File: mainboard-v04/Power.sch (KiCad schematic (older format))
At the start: 53 parts, among them Q1 IRLML2803, U17 BQ25883RGER, U4 ADM1176-1ARMZ-R7, U5 TPS54226PWPRPWP14_2P31X2P46-L, U6 LTC4121, U7 NDS8434

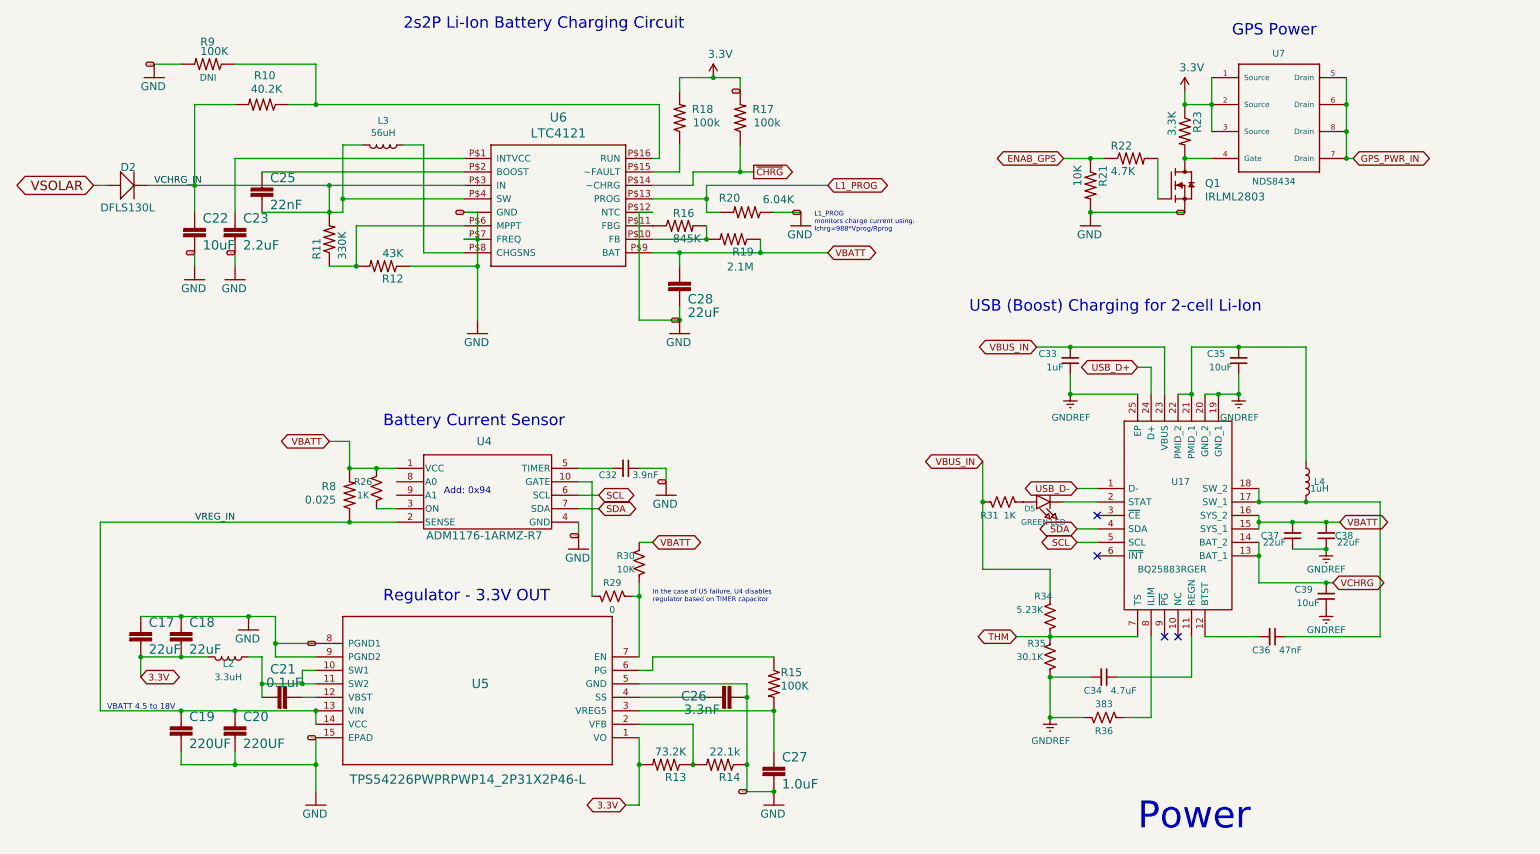
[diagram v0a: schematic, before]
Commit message: adding mainbaordv04 layout and BOM
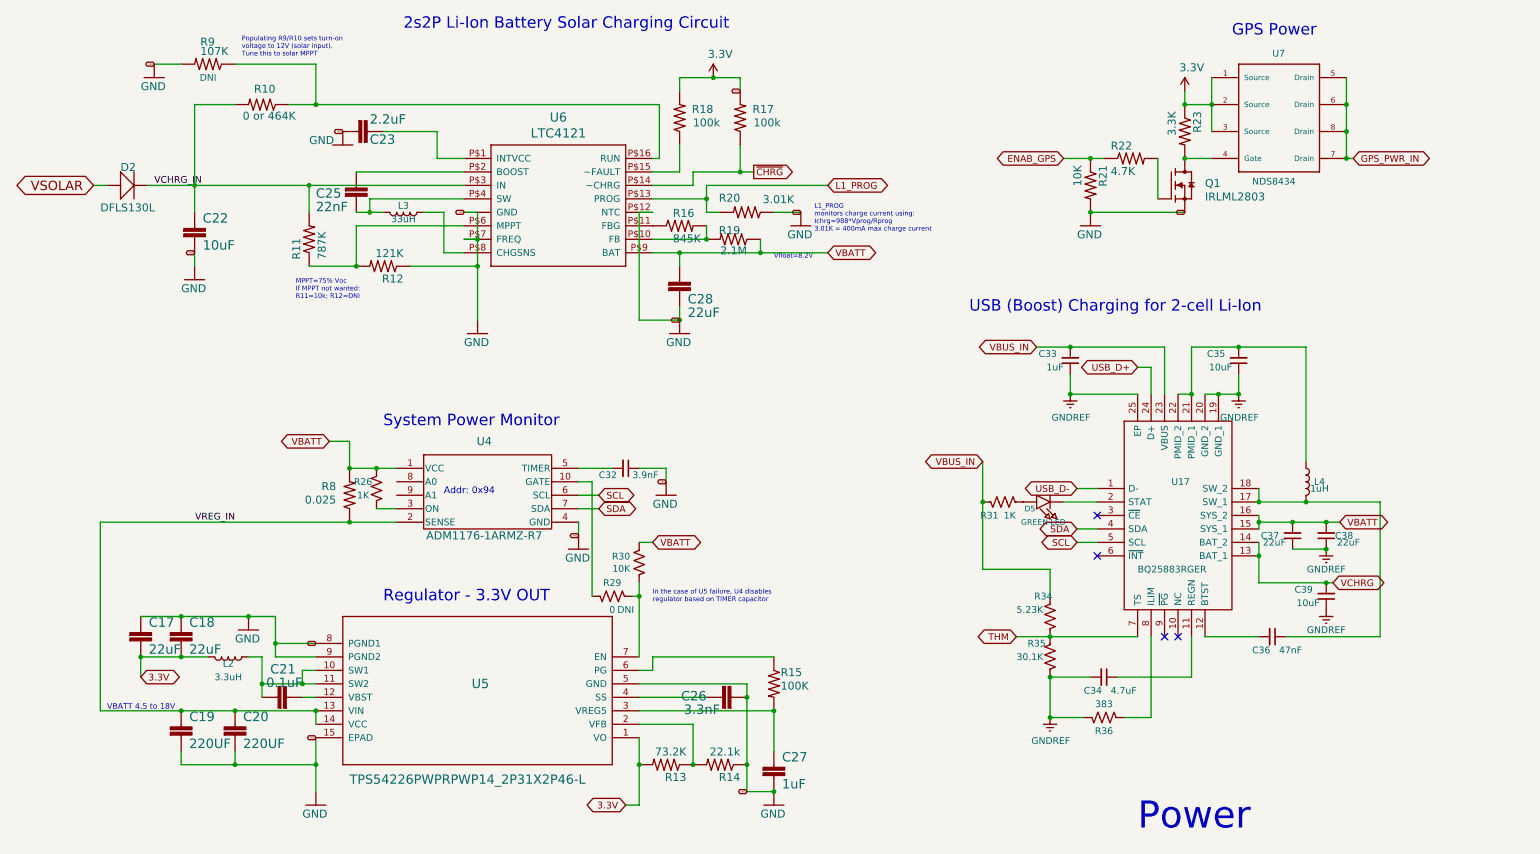
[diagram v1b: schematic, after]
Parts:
- C27: value 1.0uF -> 1uF
- D2: Flight (none) -> DFLS130L; Proto (none) -> DFLS130L
- L2: footprint Inductor_SMD:L_1812_4532Metric -> custom-footprints:L_2141
- L3: value 56uH -> 33uH
- Q1: Flight (none) -> IRLML2803; Proto (none) -> 2302
- R10: value 40.2K -> 0 or 464K
- R11: value 330K -> 787K
- R12: value 43K -> 121K
- R20: value 6.04K -> 3.01K
- R29: DNI (none) -> DNI
- R9: value 100K -> 107K
- U17: Flight (none) -> BQ25883RGER; Height 1 -> (none); Manufacturer_Name Texas Instruments -> (none); Manufacturer_Part_Number BQ25883RGER -> (none); Mouser Part Number 595-BQ25883RGER -> (none); Mouser Price/Stock https://www.mouser.com/Search/Refine.aspx?Keyword=595-BQ258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 -> (none); Proto (none) -> BQ25883RGER
- U4: Flight (none) -> ADM1176-1ARMZ-R7; Proto (none) -> ADM1176-1ARMZ-R7
- U5: Flight (none) -> TPS54226PWPRPWP14_2P31X2P46-L; Proto (none) -> TPS54226PWPRPWP14_2P31X2P46-L
- U6: Flight (none) -> LTC4121EUD; Proto (none) -> LTC4121EUD
- U7: Field4 ON Semiconductor -> (none); Field5 Unavailable -> (none); Field6 None -> (none); Field7 NDS8434 -> (none); Field8 SO-8 ON Semiconductor -> (none); Flight (none) -> NDS8434; Proto (none) -> DMP2022LSS-13
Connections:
- net VCHRG_IN: no longer C25.2, L3.2, U6.P$4 (SW)
- new net: C25.2, L3.2, U6.P$4 (SW)
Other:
- note added: "2s2P Li-Ion Battery Solar Charging Circuit"
- note added: "Addr: 0x94"
- note added: "L1_PROG\nmonitors charge current using:\nIchrg=988*Vprog/Rprog\n3.01K = 400mA max charge current\n"
- note added: "MPPT=75% Voc\nIf MPPT not wanted:\nR11=10k; R12=DNI"
- note added: "Populating R9/R10 sets turn-on\nvoltage to 12V (solar input). \nTune this to solar MPPT"
- note added: "System Power Monitor"
- note added: "Vfloat=8.2V"
- note removed: "2s2P Li-Ion Battery Charging Circuit"
- note removed: "Add: 0x94"
- note removed: "Battery Current Sensor"
- note removed: "L1_PROG\nmonitors charge current using:\nIchrg=988*Vprog/Rprog\n"
- moved on the sheet: C23, C25, L3, R11

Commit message: cleaned up v04
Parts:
- added J14: USB Jumpers, Connector_PinHeader_2.54mm:PinHeader_1x04_P2.54mm_Vertical, symbol Connector_Generic:Conn_01x04
- added R46: 10K, Resistor_SMD:R_0603_1608Metric, symbol Device:R_US
- C19, C20: value 220UF -> 100uF
- L2: Flight (none) -> SPM5030T-3R3M-HZ; Proto (none) -> HPC5040NF-3R3MTH
- L3: Flight (none) -> SLF6028T-330MR69-PF; Proto (none) -> SNR5040K-330M
- L4: footprint custom-footprints:XFL4030472MEB -> custom-footprints:L_4141; Flight (none) -> XFL4020-222ME; PN XFL4020-222ME -> (none); Proto (none) -> XFL4020-222ME
- R10: value 0 or 464K -> 0
- R11: value 787K -> 10K
- R12: DNI (none) -> DNI
- R8: value 0.025 -> 1.0
- U17: footprint QFN50P400X400X100-25N-D -> custom-footprints:QFN50P400X400X100-25N-D
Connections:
- net GNDREF: now also R46.1
- net THM: now also R46.2
- net VBATT: now also J14.2 (Pin_2); no longer C37.2, C38.2, U17.15 (SYS_1), U17.16 (SYS_2)
- net VCHRG: now also J14.4 (Pin_4); no longer C39.2, U17.13 (BAT_1), U17.14 (BAT_2)
- new net: C37.2, C38.2, J14.1 (Pin_1), U17.15 (SYS_1), U17.16 (SYS_2)
- new net: C39.2, J14.3 (Pin_3), U17.13 (BAT_1), U17.14 (BAT_2)
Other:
- note added: ""VCHRG""
- note added: ""VUSB""
- note added: "Add jumper to allow\nUSB battery charging\n(even inside P-Pod).\n"
- note added: "Add jumper to allow\nUSB to power the board\n(even inside P-Pod).\n"
- note added: "Current Sense Resistor:\n1.0 Ohm is about 0.3mW\npower lost as heat"
- note added: "In the case of U5 failure, U4 can disable\nregulator based on TIMER capacitor\n(only install this if you know what you're doing!)"
- note added: "MPPT off by default\nTo enable: MPPT=75% Voc\nR11=787K, R12=121K\nTo disable MPTT:\nR11=10k; R12=DNI"
- note added: "NOTE: Components labeled "do not install" (DNI) are not populated by default"
- note added: "Populating R9=107K,R10=464K\nsets turn-on voltage to 12V (solar input). \nTune this to solar MPPT"
- note added: "Remove both jumpers before flight to remove\nrisk of unknown BQ25883 radiation failure modes\n"
- note added: "USB Jumpers"
- note added: "VSOLAR 9V to 40V"
- note removed: "In the case of U5 failure, U4 disables\nregulator based on TIMER capacitor"
- note removed: "MPPT=75% Voc\nIf MPPT not wanted:\nR11=10k; R12=DNI"
- note removed: "Populating R9/R10 sets turn-on\nvoltage to 12V (solar input). \nTune this to solar MPPT"
- moved on the sheet: C33, C34, C35, C36, C37, C38, C39, D5, L4, R31, R34, R35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
